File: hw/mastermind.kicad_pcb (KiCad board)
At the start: 2 copper layers, 16 parts, among them J1 CONN_01X03, SW1 R13-529, SW2 R13-529, SW3 R13-529, SW4 R13-529, U1 ESP32_THING, U2 LevelShifter

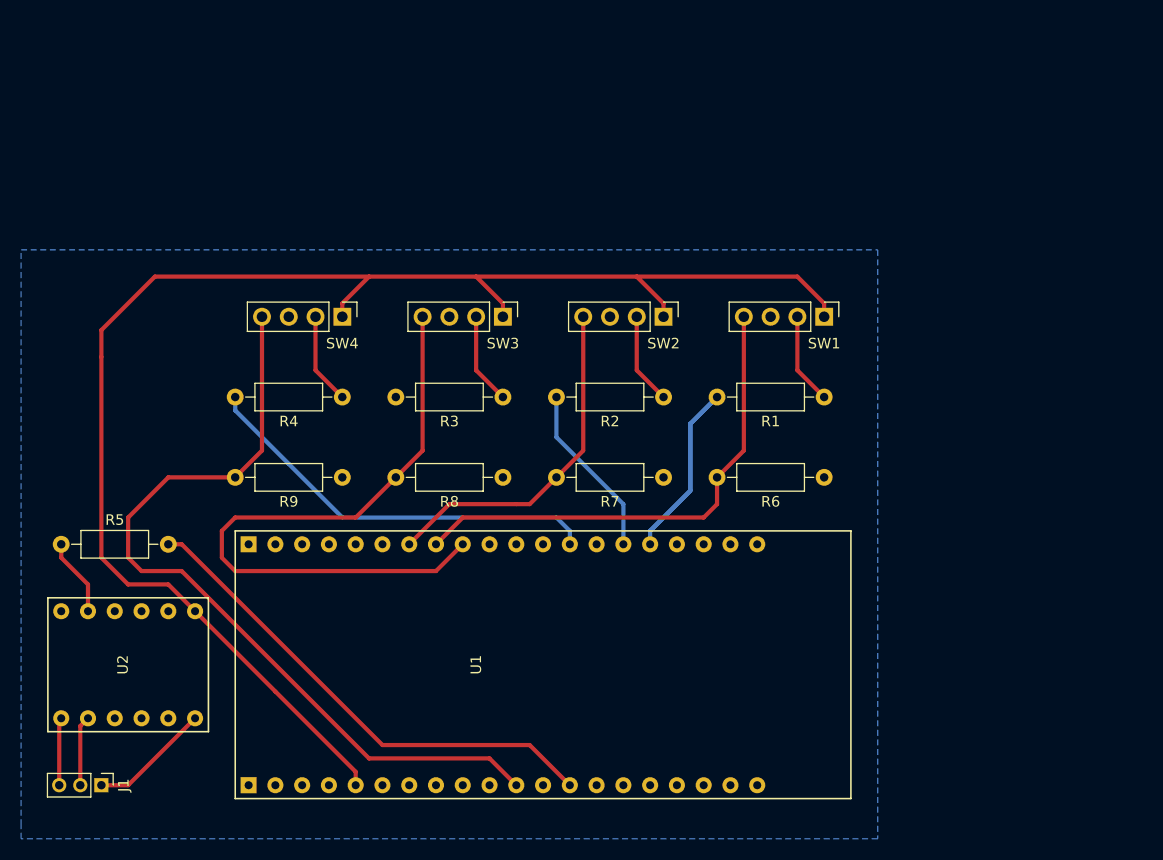
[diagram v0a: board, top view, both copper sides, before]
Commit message: redesign of the entire pcb to match physical dimensions requirements
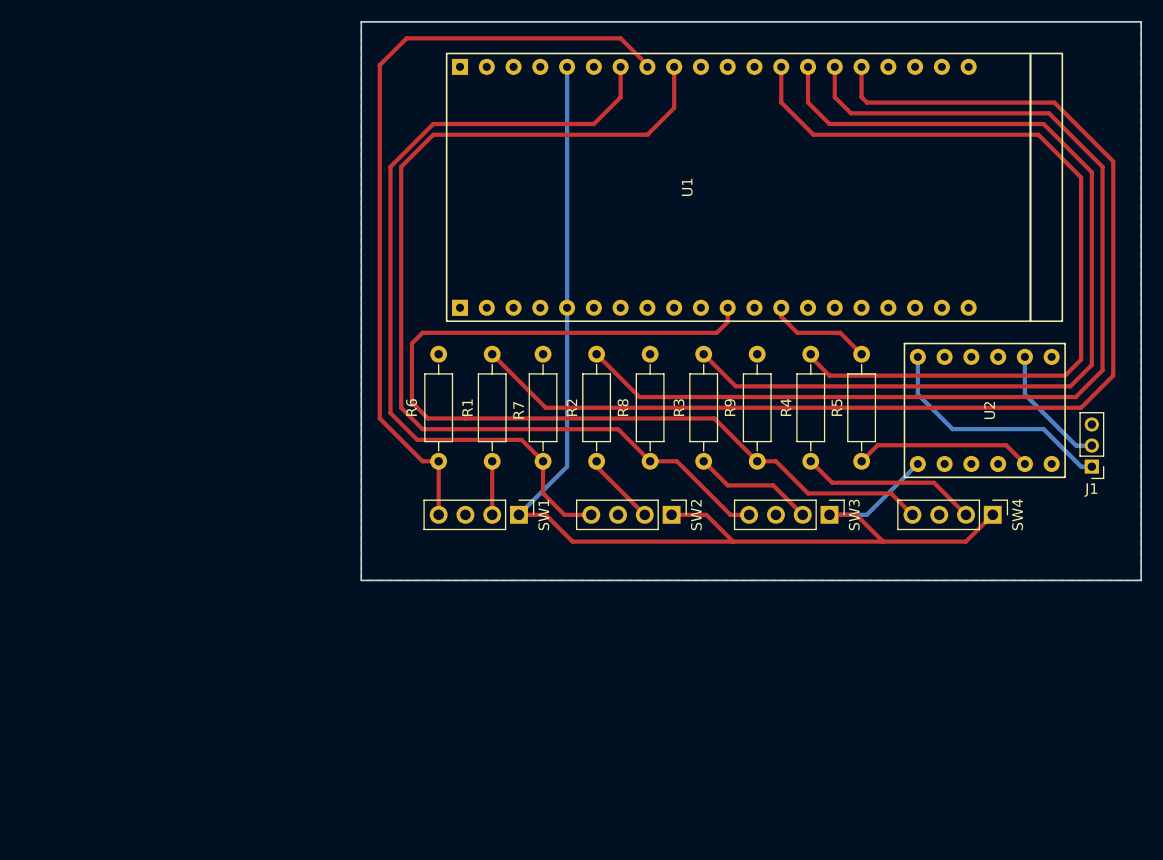
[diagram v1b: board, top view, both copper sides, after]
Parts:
- moved J1 98.7 mm to (147.3, 108.2), turned to 180 degrees
- moved U2 84.8 mm to (137.2, 102.9), turned to 90 degrees
- moved R5 76.4 mm to (125.5, 107.7), turned to 90 degrees
- moved SW4 64.5 mm to (137.9, 112.8)
- moved U1 49.5 mm to (86.1, 81.7)
- moved R4 44.9 mm to (120.7, 107.7), turned to 90 degrees
- moved R9 41.1 mm to (115.6, 97.5), turned to 270 degrees
- moved R6 38.4 mm to (85.3, 97.5), turned to 270 degrees
- moved SW3 36.2 mm to (122.4, 112.8)
- moved SW1 34.5 mm to (93.0, 112.8)
- moved R1 32.1 mm to (90.4, 107.7), turned to 90 degrees
- moved R3 20.0 mm to (110.5, 107.7), turned to 90 degrees
- moved SW2 18.8 mm to (107.4, 112.8)
- moved R8 18.2 mm to (105.4, 97.5), turned to 270 degrees
- moved R7 16.3 mm to (95.2, 97.5), turned to 270 degrees
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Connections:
- U1 pad 14: (no net) -> /LED3
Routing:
- net /LED3: track 0.00 -> 90.3 mm
- net /LED2: track 16.6 -> 101.1 mm
- net /LED1: track 31.9 -> 111.9 mm
- net /SW2: track 32.9 -> 76.0 mm
- net /LED4: track 39.0 -> 79.3 mm
- net Net-(R5-Pad2): track 47.6 -> 9.95 mm
- net /SW3: track 61.9 -> 92.4 mm
- net +3V3: track 143.0 -> 114.9 mm
- net /SW1: track 47.1 -> 73.6 mm
- net /SW4: track 77.6 -> 89.7 mm
- net VCC: track 11.5 -> 22.9 mm
- net Net-(R5-Pad1): track 7.40 -> 16.9 mm
- net Net-(R4-Pad1): track 8.67 -> 16.8 mm
- net GND: track 6.43 -> 0.00 mm
- net Net-(J1-Pad2): track 6.65 -> 11.9 mm
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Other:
- board outline added: 74 x 53 mm

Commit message: Add power input header and a few corrections
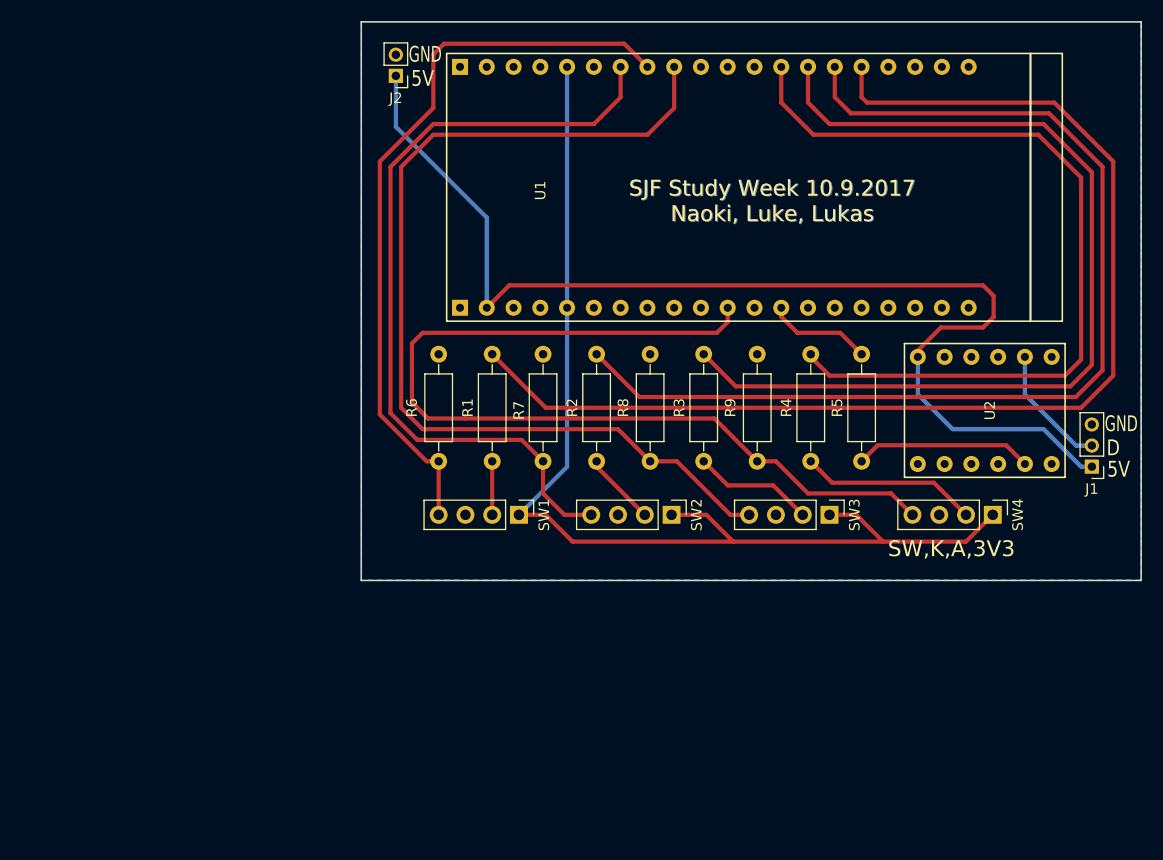
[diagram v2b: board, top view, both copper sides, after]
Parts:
- added J2: PSU_PWR, Pin_Headers:Pin_Header_Straight_1x02_Pitch2.00mm, F.Cu at (81.3, 71.1)
- J1: value CONN_01X03 -> NEOMATRIX
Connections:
- U1 pad 39: Net-(U1-Pad39) -> VCC
- U2 pad 1: +3V3 -> Net-(U2-Pad1)
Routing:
- net VCC: track 22.9 -> 109.0 mm
- net +3V3: track 114.9 -> 104.5 mm
- net /SW1: track 73.6 -> 70.7 mm
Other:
- board text added: "5V"
- board text added: "D"
- board text added: "GND"
- board text added: "SJF Study Week 10.9.2017 Naoki, Luke, Lukas"
- board text added: "SW,K,A,3V3"

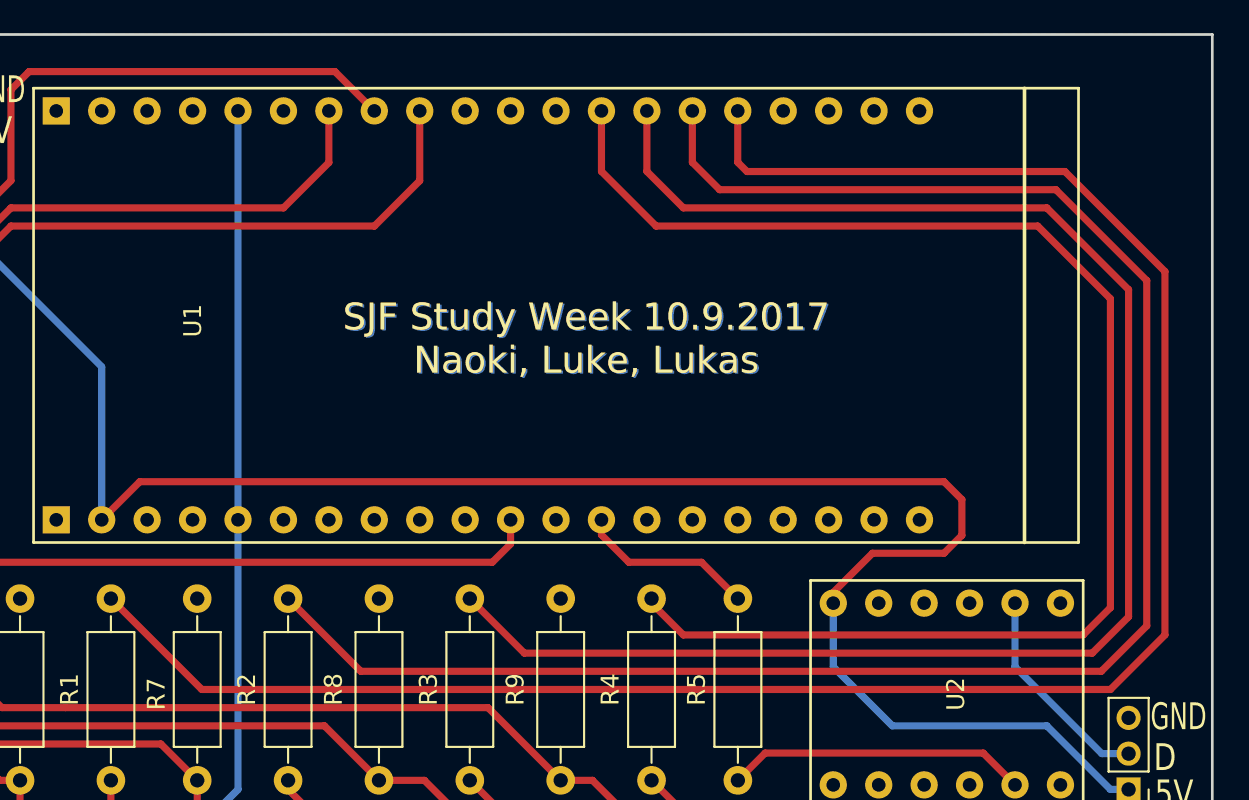
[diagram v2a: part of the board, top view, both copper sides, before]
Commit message: Redoing PCB design because there are a few mistakes
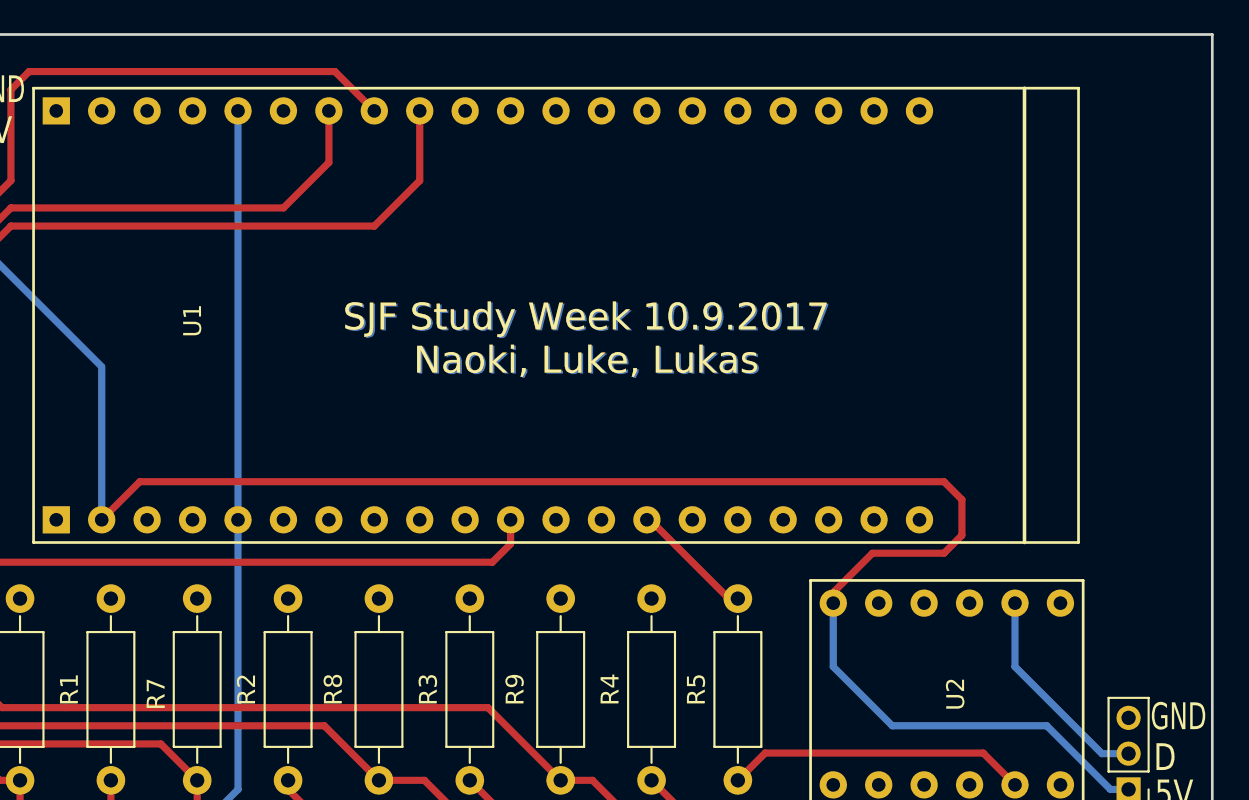
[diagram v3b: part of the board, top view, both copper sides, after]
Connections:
- R1 pad 2: /LED1 -> /LED4
- R2 pad 2: /LED2 -> /LED3
- R3 pad 2: /LED3 -> /LED2
- R4 pad 2: /LED4 -> /LED1
- U1 pad 13: /LED4 -> Net-(U1-Pad13)
- U1 pad 14: /LED3 -> Net-(U1-Pad14)
- U1 pad 15: /LED2 -> Net-(U1-Pad15)
- U1 pad 16: /LED1 -> Net-(U1-Pad16)
- U1 pad 26: Net-(U1-Pad26) -> /LED4
- U1 pad 27: Net-(U1-Pad27) -> Net-(R5-Pad2)
- U1 pad 28: Net-(R5-Pad2) -> /LED3
- U1 pad 34: Net-(U1-Pad34) -> /LED2
- U1 pad 35: Net-(U1-Pad35) -> /LED1
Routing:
- net /LED1: track 111.9 -> 0.25 mm
- net /LED2: track 101.1 -> 0.00 mm
- net /LED3: track 90.3 -> 0.00 mm
- net /LED4: track 79.3 -> 0.00 mm
- net Net-(R5-Pad2): track 9.95 -> 6.91 mm
